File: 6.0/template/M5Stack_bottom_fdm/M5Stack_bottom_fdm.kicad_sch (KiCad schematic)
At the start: 9 parts, among them U1 M-BUS

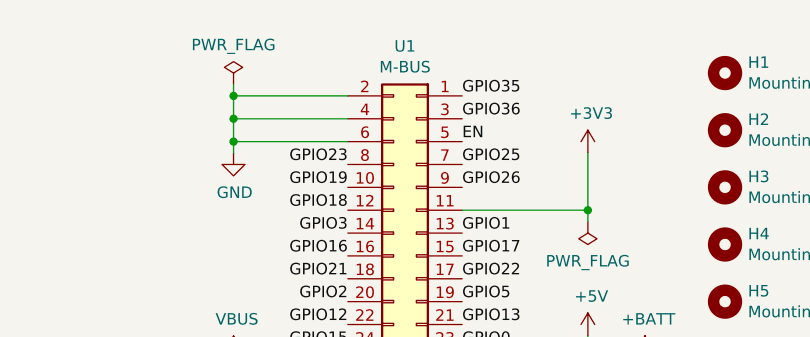
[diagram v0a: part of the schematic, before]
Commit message: template M5Stack
M-BUS connector  U1 to J1
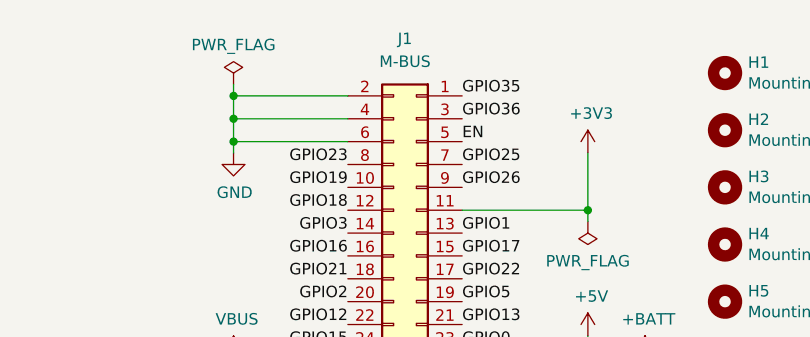
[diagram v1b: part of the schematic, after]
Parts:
- removed U1: M-BUS, @bf:BF@M5Stack_MBUS_Headder, symbol Connector_Generic:Conn_02x15_Odd_Even
- added J1: M-BUS, @bf:BF@M5Stack_MBUS_Headder, symbol Connector_Generic:Conn_02x15_Odd_Even
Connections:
- net +3V3: now also J1.11 (Pin_11)
- net +5V: now also J1.27 (Pin_27)
- net +BATT: now also J1.29 (Pin_29)
- net EN: now also J1.5 (Pin_5)
- net GND: now also J1.2 (Pin_2), J1.4 (Pin_4), J1.6 (Pin_6)
- net GPIO0: now also J1.23 (Pin_23)
- net GPIO1: now also J1.13 (Pin_13)
- net GPIO12: now also J1.22 (Pin_22)
- net GPIO13: now also J1.21 (Pin_21)
- net GPIO15: now also J1.24 (Pin_24)
- net GPIO16: now also J1.16 (Pin_16)
- net GPIO17: now also J1.15 (Pin_15)
- net GPIO18: now also J1.12 (Pin_12)
- net GPIO19: now also J1.10 (Pin_10)
- net GPIO2: now also J1.20 (Pin_20)
- net GPIO21: now also J1.18 (Pin_18)
- net GPIO22: now also J1.17 (Pin_17)
- net GPIO23: now also J1.8 (Pin_8)
- net GPIO25: now also J1.7 (Pin_7)
- net GPIO26: now also J1.9 (Pin_9)
- net GPIO3: now also J1.14 (Pin_14)
- net GPIO34: now also J1.25 (Pin_25)
- net GPIO35: now also J1.1 (Pin_1)
- net GPIO36: now also J1.3 (Pin_3)
- net GPIO5: now also J1.19 (Pin_19)
- net VBUS: now also J1.26 (Pin_26), J1.28 (Pin_28), J1.30 (Pin_30)
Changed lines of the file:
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@@
   (paper "A4")
   (title_block
-    (date "2022-10-22")
+    (date "2022-10-23")
   )
   (junction (at 212.09 21.59) (diameter 0) (color 0 0 0 0)
@@
     (pin "1")
   )
+  (symbol (lib_id "Connector_Generic:Conn_02x15_Odd_Even") (at 232.41 39.37 0) (mirror y) (unit 1)
+    (in_bom yes) (on_board yes)
+    (property "Reference" "J1" (id 0) (at 231.14 15.24 0))
+    (property "Value" "M-BUS" (id 1) (at 231.14 17.78 0))
+    (property "Footprint" "@bf:BF@M5Stack_MBUS_Headder" (id 2) (at 232.41 39.37 0)
+      (effects (font (size 1.27 1.27)) hide)
+    )
+    (property "Datasheet" "~" (id 3) (at 232.41 39.37 0)
+      (effects (font (size 1.27 1.27)) hide)
+    )
+    (pin "1")
+    (pin "10")
+    (pin "11")
+    (pin "12")
+    (pin "13")
+    (pin "14")
+    (pin "15")
+    (pin "16")
+    (pin "17")
+    (pin "18")
+    (pin "19")
+    (pin "2")
+    (pin "20")
+    (pin "21")
+    (pin "22")
+    (pin "23")
+    (pin "24")
+    (pin "25")
+    (pin "26")
+    (pin "27")
+    (pin "28")
+    (pin "29")
+    (pin "3")
+    (pin "30")
+    (pin "4")
+    (pin "5")
+    (pin "6")
+    (pin "7")
+    (pin "8")
+    (pin "9")
+  )
   (symbol (lib_id "Mechanical:MountingHole") (at 266.7 25.4 0) (unit 1)
     (in_bom yes) (on_board yes)
@@
     (pin "1")
   )
-  (symbol (lib_id "Connector_Generic:Conn_02x15_Odd_Even") (at 232.41 39.37 0) (mirror y) (unit 1)
-    (in_bom yes) (on_board yes)
-    (property "Reference" "U1" (id 0) (at 231.14 16.0782 0))
-    (property "Value" "M-BUS" (id 1) (at 231.14 18.3896 0))
-    (property "Footprint" "@bf:BF@M5Stack_MBUS_Headder" (id 2) (at 232.41 39.37 0)
-      (effects (font (size 1.27 1.27)) hide)
-    )
-    (property "Datasheet" "~" (id 3) (at 232.41 39.37 0)
-      (effects (font (size 1.27 1.27)) hide)
-    )
-    (pin "1")
-    (pin "10")
-    (pin "11")
-    (pin "12")
-    (pin "13")
-    (pin "14")
-    (pin "15")
-    (pin "16")
-    (pin "17")
-    (pin "18")
-    (pin "19")
-    (pin "2")
-    (pin "20")
-    (pin "21")
-    (pin "22")
-    (pin "23")
-    (pin "24")
-    (pin "25")
-    (pin "26")
-    (pin "27")
-    (pin "28")
-    (pin "29")
-    (pin "3")
-    (pin "30")
-    (pin "4")
-    (pin "5")
-    (pin "6")
-    (pin "7")
-    (pin "8")
-    (pin "9")
-  )
   (sheet_instances
     (path "/" (page "1"))
@@
       (reference "H8") (unit 1) (value "MountingHole") (footprint "@bf:BF@MountingHole_2.2mm_M2")
     )
-    (path "/f53ca6a9-a3d5-4b49-96ba-0af877934a36"
-      (reference "U1") (unit 1) (value "M-BUS") (footprint "@bf:BF@M5Stack_MBUS_Headder")
+    (path "/57824202-d286-4c61-a73e-67785328db94"
+      (reference "J1") (unit 1) (value "M-BUS") (footprint "@bf:BF@M5Stack_MBUS_Headder")
     )
   )
